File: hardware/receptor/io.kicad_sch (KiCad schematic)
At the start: 7 parts, among them J4 BOBINA 5V, Q1 AO3400A

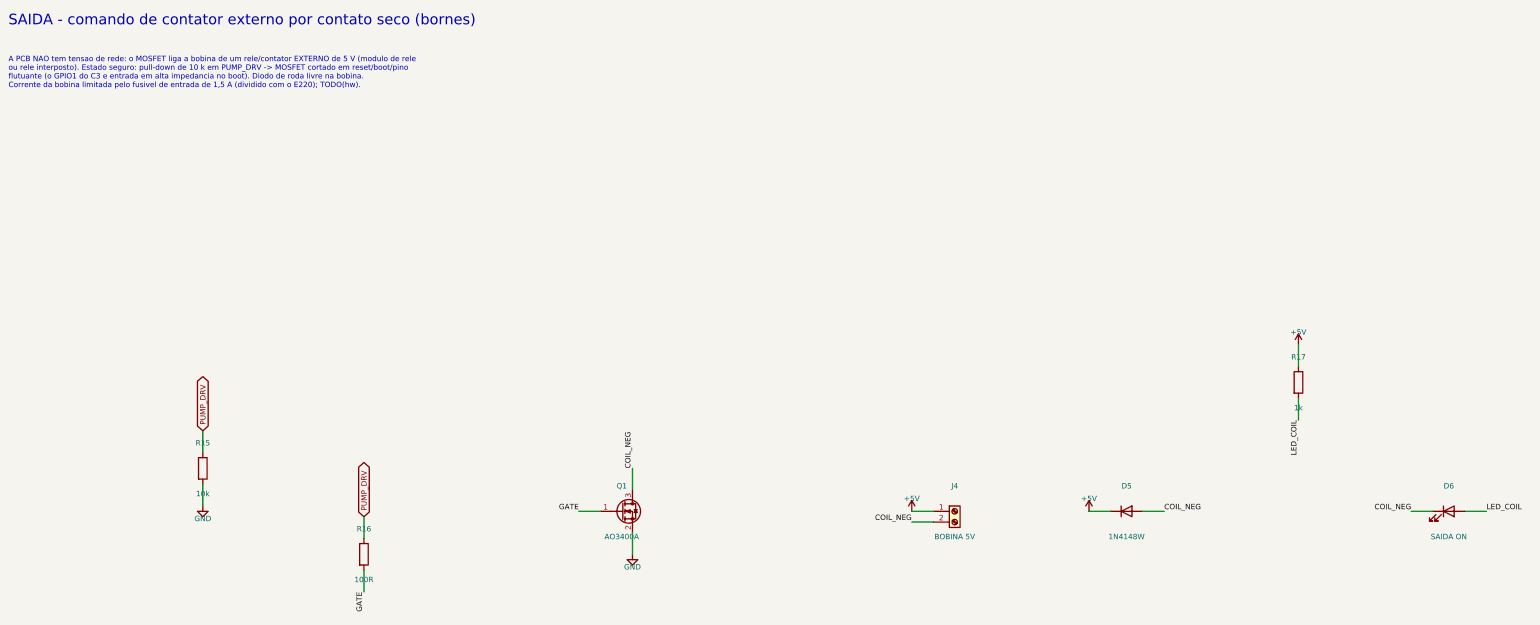
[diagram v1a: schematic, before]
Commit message: feat(hw): jack 12 V com buck AP63205, roteador proprio e serigrafia padronizada (receptor roteado; emissor com 1 net aberta)
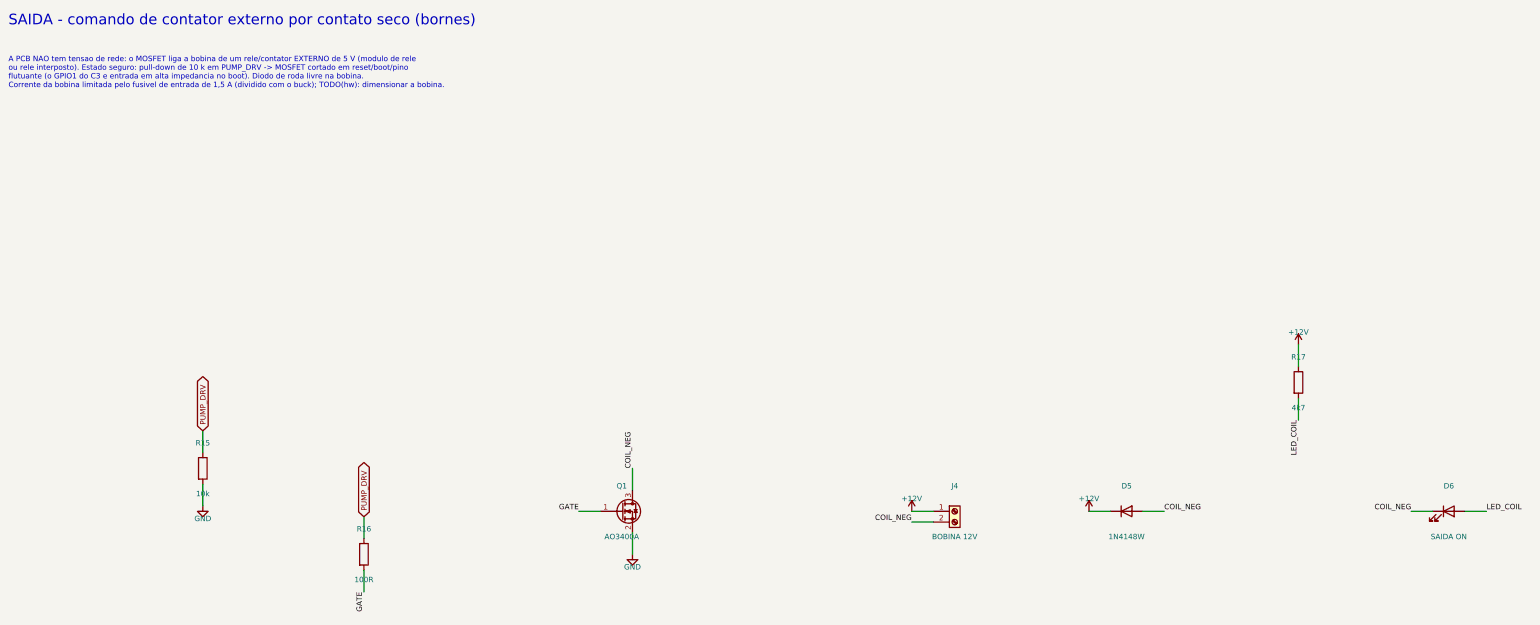
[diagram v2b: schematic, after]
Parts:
- J4: value BOBINA 5V -> BOBINA 12V
- R17: value 1k -> 4k7; MPN RC0603FR-071KL -> RC0603FR-074K7L
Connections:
- net +5V renamed +12V
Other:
- note added: "A PCB NAO tem tensao de rede: o MOSFET liga a bobina de um rele/contator EXTERNO de 5 V (modulo de rele ou rele interposto). Estado seguro: pull-down de 10 k em PUMP_DRV -> MOSFET cortado em reset/boot/pino flutuante (o GPIO1 do C3 e entrada em alta impedancia no boot). Diodo de roda livre na bobina. Corrente da bobina limitada pelo fusivel de entrada de 1,5 A (dividido com o buck); TODO(hw): dim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"
- note removed: "A PCB NAO tem tensao de rede: o MOSFET liga a bobina de um rele/contator EXTERNO de 5 V (modulo de rele ou rele interposto). Estado seguro: pull-down de 10 k em PUMP_DRV -> MOSFET cortado em reset/boot/pino flutuante (o GPIO1 do C3 e entrada em alta impedancia no boot). Diodo de roda livre na bobina. Corrente da bobina limitada pelo fusivel de entrada de 1,5 A (dividido com o E220); TODO(hw)."
